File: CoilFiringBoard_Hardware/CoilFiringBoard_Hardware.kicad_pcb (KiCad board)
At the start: 2 copper layers, 101.6 x 76.2 mm, 21 parts, among them Q1 Q_NMOS_GDS, Q2 Q_NMOS_GDS

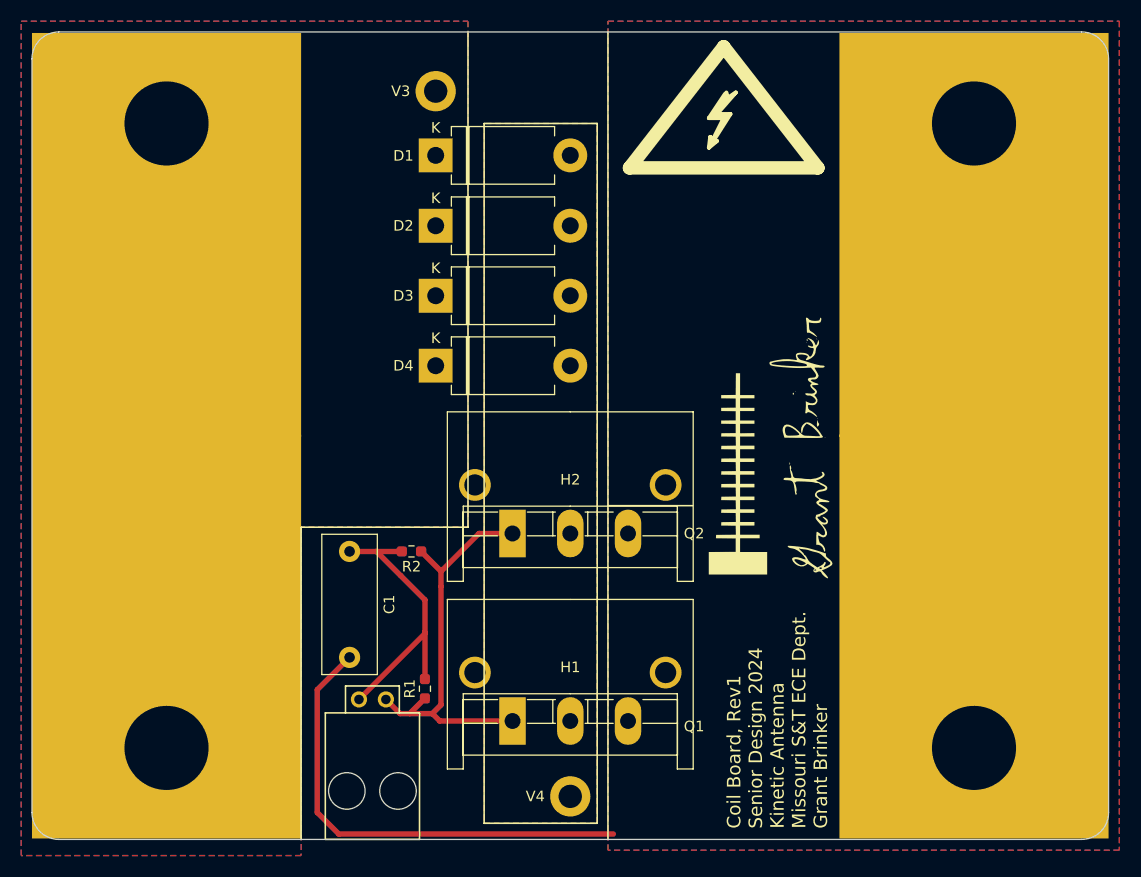
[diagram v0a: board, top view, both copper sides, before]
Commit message: Moved mounting holes + remade step and gerbs
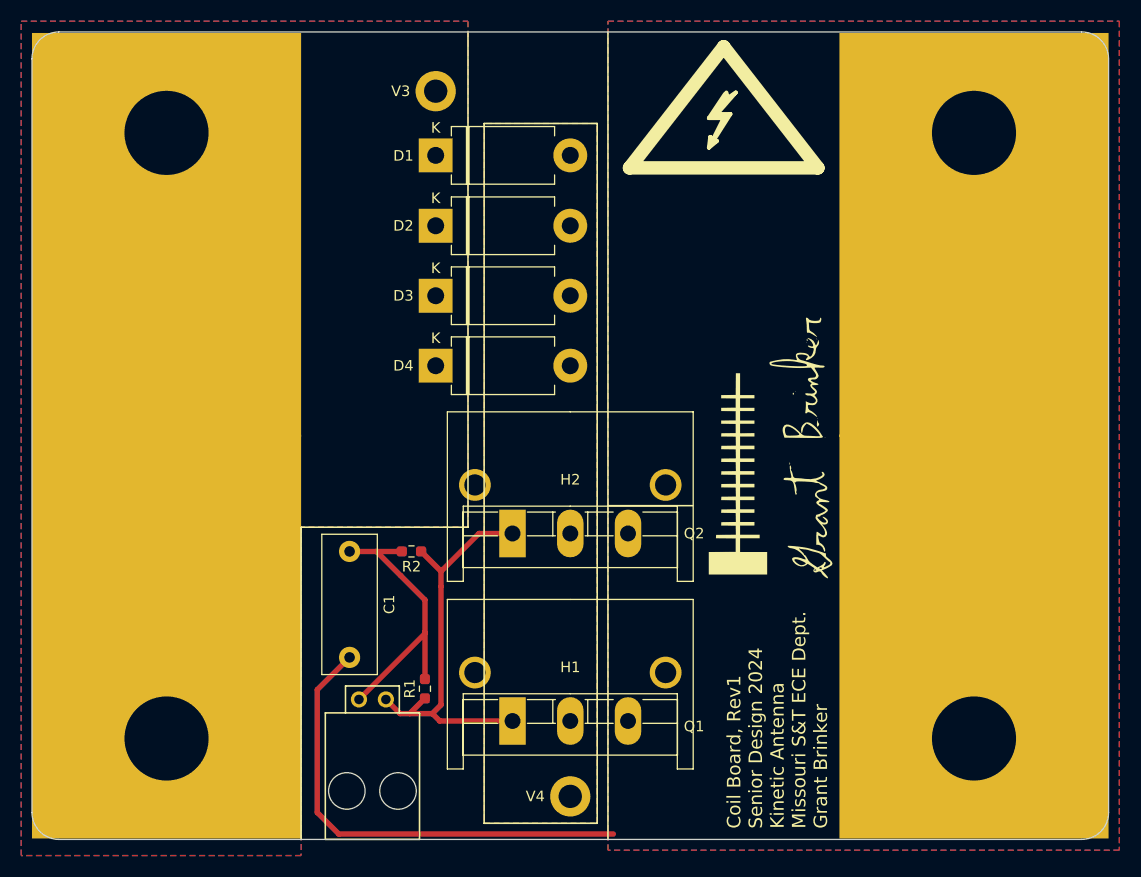
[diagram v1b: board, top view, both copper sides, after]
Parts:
- moved V1 0.89 mm to (76.2, 48.1)
- moved V2 0.89 mm to (152.4, 48.1)
- moved V5 0.89 mm to (76.2, 105.3)
- moved V6 0.89 mm to (152.4, 105.3)
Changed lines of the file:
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@@
   )
   (footprint "MRDT_Drill_Holes:BATT_PWR_VIA" (layer "F.Cu")
-    (at 76.2 106.172)
+    (at 76.2 105.283)
     (property "Sheetfile" "CoilFiringBoard_Hardware.kicad_sch")
     (property "Sheetname" "")
@@
         (effects (font (size 1 1) (thickness 0.15)))
     )
-    (pad "1" thru_hole rect (at 0 0) (size 25.4 38.1) (drill 7.9375 (offset 0 -10.50925)) (layers "*.Cu" "*.Mask")
+    (pad "1" thru_hole rect (at 0 0) (size 25.4 38.1) (drill 7.9375 (offset 0 -9.62025)) (layers "*.Cu" "*.Mask")
       (net 3 "PWR") (pintype "input") (zone_connect 2))
   )
@@
   )
   (footprint "MRDT_Drill_Holes:BATT_PWR_VIA" (layer "F.Cu")
-    (at 152.4 47.244)
+    (at 152.4 48.133)
     (property "Sheetfile" "CoilFiringBoard_Hardware.kicad_sch")
     (property "Sheetname" "")
@@
         (effects (font (size 1 1) (thickness 0.15)))
     )
-    (pad "1" thru_hole rect (at 0 0) (size 25.4 38.1) (drill 7.9375 (offset 0 10.50925)) (layers "*.Cu" "*.Mask")
+    (pad "1" thru_hole rect (at 0 0) (size 25.4 38.1) (drill 7.9375 (offset 0 9.62025)) (layers "*.Cu" "*.Mask")
       (net 4 "GND") (pintype "input") (zone_connect 2))
   )
@@
   )
   (footprint "MRDT_Drill_Holes:BATT_PWR_VIA" (layer "F.Cu")
-    (at 76.2 47.244)
+    (at 76.2 48.133)
     (property "Sheetfile" "CoilFiringBoard_Hardware.kicad_sch")
     (property "Sheetname" "")
@@
         (effects (font (size 1 1) (thickness 0.15)))
     )
-    (pad "1" thru_hole rect (at 0 0) (size 25.4 38.1) (drill 7.9375 (offset 0 10.50925)) (layers "*.Cu" "*.Mask")
+    (pad "1" thru_hole rect (at 0 0) (size 25.4 38.1) (drill 7.9375 (offset 0 9.62025)) (layers "*.Cu" "*.Mask")
       (net 3 "PWR") (pintype "input") (zone_connect 2))
   )
@@
   )
   (footprint "MRDT_Drill_Holes:BATT_PWR_VIA" (layer "F.Cu")
-    (at 152.4 106.172)
+    (at 152.4 105.283)
     (property "Sheetfile" "CoilFiringBoard_Hardware.kicad_sch")
     (property "Sheetname" "")
@@
         (effects (font (size 1 1) (thickness 0.15)))
     )
-    (pad "1" thru_hole rect (at 0 0) (size 25.4 38.1) (drill 7.9375 (offset 0 -10.50925)) (layers "*.Cu" "*.Mask")
+    (pad "1" thru_hole rect (at 0 0) (size 25.4 38.1) (drill 7.9375 (offset 0 -9.62025)) (layers "*.Cu" "*.Mask")
       (net 4 "GND") (pintype "input") (zone_connect 2))
   )
@@
   )
   (dimension (type aligned) (layer "User.1")
+    (pts (xy 76.2 48.133) (xy 76.2 105.283))
+    (height 16.002)
+    (gr_text "2250.0000 mils" (at 59.048 76.708 90) (layer "User.1")
+      (effects (font (size 1 1) (thickness 0.15)))
+    )
+    (format (prefix "") (suffix "") (units 3) (units_format 1) (precision 4))
+    (style (thickness 0.15) (arrow_length 1.27) (text_position_mode 0) (extension_height 0.58642) (extension_offset 0.5) keep_text_aligned)
+  )
+  (dimension (type aligned) (layer "User.1")
